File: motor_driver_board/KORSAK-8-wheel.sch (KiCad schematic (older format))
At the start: 26 parts, among them J1 Battery, J2 5V connector, J3 Logic Connector, J4 Charge Indicator, M1 Motor_DC, M2 Motor_DC, M3 Motor_DC, M4 Motor_DC, M5 Motor_DC, M6 Motor_DC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

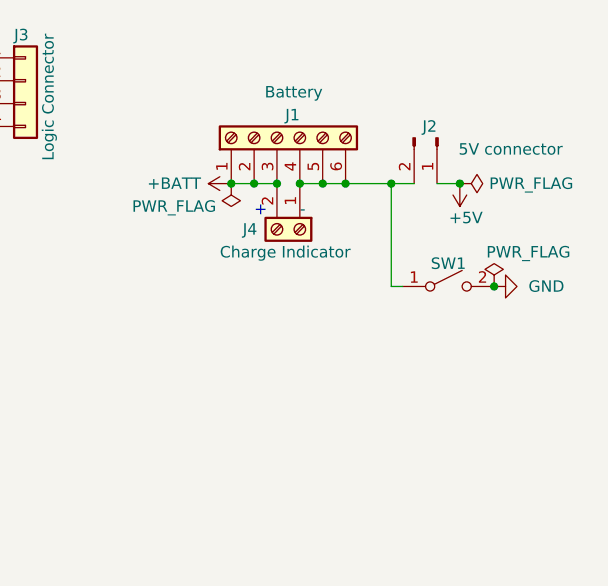
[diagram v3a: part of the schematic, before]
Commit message: Добавил вывод под зарядник
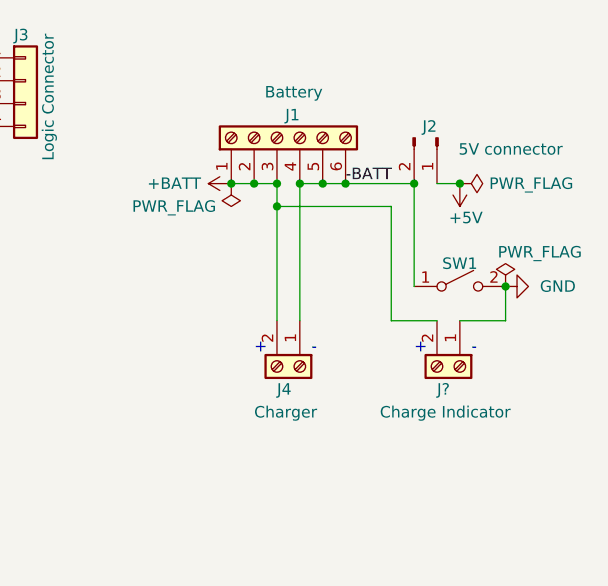
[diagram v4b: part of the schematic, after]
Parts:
- added J?: Charge Indicator, TerminalBlock_Phoenix:TerminalBlock_Phoenix_MKDS-1,5-2_1x02_P5.00mm_Horizontal, symbol Connector:Screw_Terminal_01x02
- J4: value Charge Indicator -> Charger
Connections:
- net +BATT: now also J?.2 (Pin_2)
- net GND: now also J?.1 (Pin_1)
- net -BATT: now reaches J1.4 (Pin_4), J1.5 (Pin_5), J1.6 (Pin_6), J2.2 (Pin_2), J4.1 (Pin_1), SW1.1 (A)
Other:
- moved on the sheet: J4, SW1
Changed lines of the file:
@@
 Title "KORSAK Motor Driver board"
 Date "2021-03-14"
-Rev "7"
+Rev "8"
 Comp ""
 Comment1 ""
@@
 L power:GND #PWR04
 U 1 1 5FFD08AA
-P 10200 4800
-F 0 "#PWR04" H 10200 4550 50  0001 C CNN
-F 1 "GND" V 10200 4650 50  0000 R CNN
-F 2 "" H 10200 4800 50  0001 C CNN
-F 3 "" H 10200 4800 50  0001 C CNN
-	1    10200 4800
+P 10250 4800
+F 0 "#PWR04" H 10250 4550 50  0001 C CNN
+F 1 "GND" V 10250 4650 50  0000 R CNN
+F 2 "" H 10250 4800 50  0001 C CNN
+F 3 "" H 10250 4800 50  0001 C CNN
+	1    10250 4800
 	0    -1   -1   0
 $EndComp
@@
 	4600 4900 4800 4900
 Connection ~ 9550 4350
-Connection ~ 9750 4350
-Wire Wire Line
-	9750 4350 9550 4350
+Connection ~ 9850 4350
+Wire Wire Line
+	9850 4350 9550 4350
 $Comp
 L power:PWR_FLAG #FLG0101
@@
 L power:PWR_FLAG #FLG0103
 U 1 1 60AE12BA
-P 10200 4800
-F 0 "#FLG0103" H 10200 4875 50  0001 C CNN
-F 1 "PWR_FLAG" H 10350 4950 50  0000 C CNN
-F 2 "" H 10200 4800 50  0001 C CNN
-F 3 "~" H 10200 4800 50  0001 C CNN
-	1    10200 4800
-	1    0    0    -1
-$EndComp
-Wire Wire Line
-	9750 4350 9850 4350
+P 10250 4800
+F 0 "#FLG0103" H 10250 4875 50  0001 C CNN
+F 1 "PWR_FLAG" H 10400 4950 50  0000 C CNN
+F 2 "" H 10250 4800 50  0001 C CNN
+F 3 "~" H 10250 4800 50  0001 C CNN
+	1    10250 4800
+	1    0    0    -1
+$EndComp
 $Comp
 L Switch:SW_SPST SW1
 U 1 1 604F19B3
-P 10000 4800
-F 0 "SW1" H 10000 4900 50  0000 C CNN
-F 1 "SW_SPST" H 10000 4700 50  0001 C CNN
-F 2 "TerminalBlock_Phoenix:TerminalBlock_Phoenix_MKDS-1,5-2_1x02_P5.00mm_Horizontal" H 10000 4800 50  0001 C CNN
-F 3 "~" H 10000 4800 50  0001 C CNN
-	1    10000 4800
-	1    0    0    -1
-$EndComp
-Connection ~ 9250 4350
-Connection ~ 10200 4800
-Wire Wire Line
-	9750 4350 9750 4800
-Wire Wire Line
-	9750 4800 9800 4800
+P 10050 4800
+F 0 "SW1" H 10050 4900 50  0000 C CNN
+F 1 "SW_SPST" H 10050 4700 50  0001 C CNN
+F 2 "TerminalBlock_Phoenix:TerminalBlock_Phoenix_MKDS-1,5-2_1x02_P5.00mm_Horizontal" H 10050 4800 50  0001 C CNN
+F 3 "~" H 10050 4800 50  0001 C CNN
+	1    10050 4800
+	1    0    0    -1
+$EndComp
+Connection ~ 10250 4800
+Wire Wire Line
+	9850 4350 9850 4800
 $Comp
 L Connector:Screw_Terminal_01x02 J4
 U 1 1 6053A604
-P 9350 4550
-F 0 "J4" V 9350 4300 50  0000 L CNN
-F 1 "Charge Indicator" V 9450 4200 50  0000 L CNN
-F 2 "TerminalBlock_Phoenix:TerminalBlock_Phoenix_MKDS-1,5-2_1x02_P5.00mm_Horizontal" H 9350 4550 50  0001 C CNN
-F 3 "~" H 9350 4550 50  0001 C CNN
-	1    9350 4550
+P 9350 5150
+F 0 "J4" V 9450 5050 50  0000 L CNN
+F 1 "Charger" V 9550 4950 50  0000 L CNN
+F 2 "TerminalBlock_Phoenix:TerminalBlock_Phoenix_MKDS-1,5-2_1x02_P5.00mm_Horizontal" H 9350 5150 50  0001 C CNN
+F 3 "~" H 9350 5150 50  0001 C CNN
+	1    9350 5150
 	0    1    1    0
 $EndComp
-Connection ~ 9350 4350
-Text Notes 9350 4500 0    50   ~ 0
+Text Notes 10100 5100 0    50   ~ 0
 -
-Text Notes 9150 4500 0    50   ~ 0
+Text Notes 9850 5100 0    50   ~ 0
 +
 Wire Wire Line
@@
 Text Label 7950 4100 2    50   ~ 0
 R_IN_1
+Text Label 9550 4350 0    50   ~ 0
+-BATT
+$Comp
+L Connector:Screw_Terminal_01x02 J?
+U 1 1 609ED073
+P 10050 5150
+F 0 "J?" V 10150 5050 50  0000 L CNN
+F 1 "Charge Indicator" V 10250 4800 50  0000 L CNN
+F 2 "TerminalBlock_Phoenix:TerminalBlock_Phoenix_MKDS-1,5-2_1x02_P5.00mm_Horizontal" H 10050 5150 50  0001 C CNN
+F 3 "~" H 10050 5150 50  0001 C CNN
+	1    10050 5150
+	0    1    1    0
+$EndComp
+Wire Wire Line
+	10250 4800 10250 4950
+Wire Wire Line
+	10250 4950 10050 4950
+Wire Wire Line
+	9950 4950 9750 4950
+Wire Wire Line
+	9750 4950 9750 4450
+Wire Wire Line
+	9750 4450 9250 4450
+Wire Wire Line
+	9250 4450 9250 4350
+Connection ~ 9250 4350
+Wire Wire Line
+	9250 4950 9250 4450
+Connection ~ 9250 4450
+Wire Wire Line
+	9350 4950 9350 4350
+Connection ~ 9350 4350
+Text Notes 9150 5100 0    50   ~ 0
++
+Text Notes 9400 5100 0    50   ~ 0
+-
 $EndSCHEMATC

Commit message: Закончил моделировать плату
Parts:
- removed J2: 5V connector, Connector_PinHeader_2.54mm:PinHeader_1x02_P2.54mm_Horizontal, symbol Connector:Conn_01x02_Male
- added J2: 5V Power, TerminalBlock_Phoenix:TerminalBlock_Phoenix_MKDS-1,5-2_1x02_P5.00mm_Horizontal, symbol Connector:Screw_Terminal_01x02
- added unit 7 of U5
- gave numbers to parts that had none: 1
- renumbered C5 to C3, C6 to C4, C3 to C5, C4 to C6, U4 to U2, U2 to U4
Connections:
- net +5V: now also J2.2 (Pin_2), U5.14 (VCC)
- net -BATT: now also J2.1 (Pin_1)
- net GND: now also U5.7 (GND)
- net L_IN_1: now also U3.15 (4A), U4.15 (4A); no longer U3.10 (3A), U4.10 (3A)
- net L_IN_2: now also U3.10 (3A), U4.10 (3A); no longer U3.15 (4A), U4.15 (4A)
- net M5_OUT_1: now also C6.2, M6.1 (+); no longer C5.2, M5.1 (+)
- net M5_OUT_2: now also C6.1, M6.2 (-); no longer C5.1, M5.2 (-)
- net M6_OUT_1: now also C5.2, M5.1 (+); no longer C6.2, M6.1 (+)
- net M6_OUT_2: now also C5.1, M5.2 (-); no longer C6.1, M6.2 (-)
- net M7_OUT_1: now also C8.2, M8.1 (+); no longer C7.2, M7.1 (+)
- net M7_OUT_2: now also C8.1, M8.2 (-); no longer C7.1, M7.2 (-)
- net M8_OUT_1: now also C7.2, M7.1 (+); no longer C8.2, M8.1 (+)
- net M8_OUT_2: now also C7.1, M7.2 (-); no longer C8.1, M8.2 (-)
- net R_IN_1: now also U1.15 (4A), U2.15 (4A); no longer U1.10 (3A), U2.10 (3A)
- net R_IN_2: now also U1.10 (3A), U2.10 (3A); no longer U1.15 (4A), U2.15 (4A)
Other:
- moved on the sheet: C5, C6, C7, C8, M5, M6, M7, M8
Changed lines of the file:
@@
 L Motor:Motor_DC M8
 U 1 1 601FA19C
+P 5550 5500
+F 0 "M8" V 5350 5400 50  0000 L CNN
+F 1 "Motor_DC" V 5750 5300 50  0000 L CNN
+F 2 "TerminalBlock_Phoenix:TerminalBlock_Phoenix_MKDS-1,5-2_1x02_P5.00mm_Horizontal" H 5550 5410 50  0001 C CNN
+F 3 "~" H 5550 5410 50  0001 C CNN
+	1    5550 5500
+	1    0    0    -1
+$EndComp
+$Comp
+L Motor:Motor_DC M7
+U 1 1 601FA1A6
 P 5550 4900
-F 0 "M8" V 5350 4800 50  0000 L CNN
+F 0 "M7" V 5350 4800 50  0000 L CNN
 F 1 "Motor_DC" V 5750 4700 50  0000 L CNN
 F 2 "TerminalBlock_Phoenix:TerminalBlock_Phoenix_MKDS-1,5-2_1x02_P5.00mm_Horizontal" H 5550 4810 50  0001 C CNN
 F 3 "~" H 5550 4810 50  0001 C CNN
 	1    5550 4900
-	1    0    0    -1
-$EndComp
-$Comp
-L Motor:Motor_DC M7
-U 1 1 601FA1A6
-P 5550 5500
-F 0 "M7" V 5350 5400 50  0000 L CNN
-F 1 "Motor_DC" V 5750 5300 50  0000 L CNN
-F 2 "TerminalBlock_Phoenix:TerminalBlock_Phoenix_MKDS-1,5-2_1x02_P5.00mm_Horizontal" H 5550 5410 50  0001 C CNN
-F 3 "~" H 5550 5410 50  0001 C CNN
-	1    5550 5500
 	1    0    0    -1
 $EndComp
@@
 $EndComp
 $Comp
-L Driver_Motor:L293D U2
+L Driver_Motor:L293D U4
 U 1 1 601FA21D
 P 4100 5300
-F 0 "U2" H 4250 5600 50  0000 C CNN
+F 0 "U4" H 4250 5600 50  0000 C CNN
 F 1 "L293D" H 4250 5450 50  0000 C CNN
 F 2 "Package_DIP:DIP-16_W7.62mm_Socket_LongPads" H 4350 4550 50  0001 L CNN
@@
 	1    4100 5300
 	1    0    0    -1
-$EndComp
-$Comp
-L Connector:Conn_01x02_Male J2
-U 1 1 60435B47
-P 9950 4150
-F 0 "J2" V 9900 4150 50  0000 R CNN
-F 1 "5V connector" V 10000 4700 50  0000 R CNN
-F 2 "Connector_PinHeader_2.54mm:PinHeader_1x02_P2.54mm_Horizontal" H 9950 4150 50  0001 C CNN
-F 3 "~" H 9950 4150 50  0001 C CNN
-	1    9950 4150
-	0    1    1    0
 $EndComp
 Wire Wire Line
@@
 L Device:C C7
 U 1 1 60A139F7
+P 5000 4950
+F 0 "C7" H 5115 4996 50  0000 L CNN
+F 1 "10pF" H 5115 4905 50  0000 L CNN
+F 2 "Capacitor_THT:C_Disc_D5.0mm_W2.5mm_P5.00mm" H 5038 4800 50  0001 C CNN
+F 3 "~" H 5000 4950 50  0001 C CNN
+	1    5000 4950
+	1    0    0    1
+$EndComp
+$Comp
+L Device:C C8
+U 1 1 60A183A3
 P 5000 5550
-F 0 "C7" H 5115 5596 50  0000 L CNN
+F 0 "C8" H 5115 5596 50  0000 L CNN
 F 1 "10pF" H 5115 5505 50  0000 L CNN
 F 2 "Capacitor_THT:C_Disc_D5.0mm_W2.5mm_P5.00mm" H 5038 5400 50  0001 C CNN
@@
 	1    0    0    1
 $EndComp
-$Comp
-L Device:C C8
-U 1 1 60A183A3
-P 5000 4950
-F 0 "C8" H 5115 4996 50  0000 L CNN
-F 1 "10pF" H 5115 4905 50  0000 L CNN
-F 2 "Capacitor_THT:C_Disc_D5.0mm_W2.5mm_P5.00mm" H 5038 4800 50  0001 C CNN
-F 3 "~" H 5000 4950 50  0001 C CNN
-	1    5000 4950
-	1    0    0    1
-$EndComp
 Wire Wire Line
 	5000 5700 5000 5800
@@
 	4600 4900 4800 4900
 Connection ~ 9550 4350
-Connection ~ 9850 4350
 Wire Wire Line
 	9850 4350 9550 4350
@@
 	1550 5300 1000 5300
 Connection ~ 1550 5300
-Wire Wire Line
-	1550 5400 1550 5300
 $Comp
 L Device:C C1
@@
 $EndComp
 $Comp
-L Device:C C3
+L Device:C C5
 U 1 1 60A267CC
+P 1550 4950
+F 0 "C5" H 1665 4996 50  0000 L CNN
+F 1 "10pF" H 1665 4905 50  0000 L CNN
+F 2 "Capacitor_THT:C_Disc_D5.0mm_W2.5mm_P5.00mm" H 1588 4800 50  0001 C CNN
+F 3 "~" H 1550 4950 50  0001 C CNN
+	1    1550 4950
+	-1   0    0    1
+$EndComp
+$Comp
+L Device:C C6
+U 1 1 60A1E5A3
 P 1550 5550
-F 0 "C3" H 1665 5596 50  0000 L CNN
+F 0 "C6" H 1665 5596 50  0000 L CNN
 F 1 "10pF" H 1665 5505 50  0000 L CNN
 F 2 "Capacitor_THT:C_Disc_D5.0mm_W2.5mm_P5.00mm" H 1588 5400 50  0001 C CNN
 F 3 "~" H 1550 5550 50  0001 C CNN
 	1    1550 5550
-	-1   0    0    1
-$EndComp
-$Comp
-L Device:C C4
-U 1 1 60A1E5A3
-P 1550 4950
-F 0 "C4" H 1665 4996 50  0000 L CNN
-F 1 "10pF" H 1665 4905 50  0000 L CNN
-F 2 "Capacitor_THT:C_Disc_D5.0mm_W2.5mm_P5.00mm" H 1588 4800 50  0001 C CNN
-F 3 "~" H 1550 4950 50  0001 C CNN
-	1    1550 4950
 	-1   0    0    1
 $EndComp
@@
 L Motor:Motor_DC M6
 U 1 1 601FA1F2
-P 1000 4900
-F 0 "M6" V 1200 4800 50  0000 L CNN
-F 1 "Motor_DC" V 800 4700 50  0000 L CNN
-F 2 "TerminalBlock_Phoenix:TerminalBlock_Phoenix_MKDS-1,5-2_1x02_P5.00mm_Horizontal" H 1000 4810 50  0001 C CNN
-F 3 "~" H 1000 4810 50  0001 C CNN
-	1    1000 4900
+P 1000 5500
+F 0 "M6" V 1200 5400 50  0000 L CNN
+F 1 "Motor_DC" V 800 5300 50  0000 L CNN
+F 2 "TerminalBlock_Phoenix:TerminalBlock_Phoenix_MKDS-1,5-2_1x02_P5.00mm_Horizontal" H 1000 5410 50  0001 C CNN
+F 3 "~" H 1000 5410 50  0001 C CNN
+	1    1000 5500
 	1    0    0    -1
 $EndComp
@@
 L Motor:Motor_DC M5
 U 1 1 601FA1E8
-P 1000 5500
-F 0 "M5" V 800 5400 50  0000 L CNN
-F 1 "Motor_DC" V 1200 5300 50  0000 L CNN
-F 2 "TerminalBlock_Phoenix:TerminalBlock_Phoenix_MKDS-1,5-2_1x02_P5.00mm_Horizontal" H 1000 5410 50  0001 C CNN
-F 3 "~" H 1000 5410 50  0001 C CNN
-	1    1000 5500
+P 1000 4900
+F 0 "M5" V 800 4800 50  0000 L CNN
+F 1 "Motor_DC" V 1200 4700 50  0000 L CNN
+F 2 "TerminalBlock_Phoenix:TerminalBlock_Phoenix_MKDS-1,5-2_1x02_P5.00mm_Horizontal" H 1000 4810 50  0001 C CNN
+F 3 "~" H 1000 4810 50  0001 C CNN
+	1    1000 4900
 	-1   0    0    -1
 $EndComp
@@
 Wire Wire Line
 	2950 5700 3600 5700
-Text Label 3150 5300 0    50   ~ 0
+Text Label 3150 5500 0    50   ~ 0
 L_IN_1
 Text Label 3150 4700 0    50   ~ 0
@@
 Text Label 3150 4900 0    50   ~ 0
 L_IN_2
-Text Label 3150 5500 0    50   ~ 0
+Text Label 3150 5300 0    50   ~ 0
 L_IN_2
 Text Label 3150 5700 0    50   ~ 0
@@
 Text Label 3150 2350 0    50   ~ 0
 R_IN_1
-Text Label 3150 2950 0    50   ~ 0
+Text Label 3150 3150 0    50   ~ 0
 R_IN_1
 Text Label 3150 2550 0    50   ~ 0
 R_IN_2
-Text Label 3150 3150 0    50   ~ 0
+Text Label 3150 2950 0    50   ~ 0
 R_IN_2
 $Comp
@@
 	5000 2950 5000 3050
 $Comp
-L Device:C C6
+L Device:C C4
 U 1 1 60A02B64
 P 5000 3200
-F 0 "C6" H 5115 3246 50  0000 L CNN
+F 0 "C4" H 5115 3246 50  0000 L CNN
 F 1 "10pF" H 5115 3155 50  0000 L CNN
 F 2 "Capacitor_THT:C_Disc_D5.0mm_W2.5mm_P5.00mm" H 5038 3050 50  0001 C CNN
@@
 	5000 2750 5000 2850
 $Comp
-L Device:C C5
+L Device:C C3
 U 1 1 609F73D7
 P 5000 2600
-F 0 "C5" H 5115 2646 50  0000 L CNN
+F 0 "C3" H 5115 2646 50  0000 L CNN
 F 1 "10pF" H 5115 2555 50  0000 L CNN
 F 2 "Capacitor_THT:C_Disc_D5.0mm_W2.5mm_P5.00mm" H 5038 2450 50  0001 C CNN
@@
 	4800 2550 4800 2850
 $Comp
-L Driver_Motor:L293D U4
+L Driver_Motor:L293D U2
 U 1 1 5F9AC5A8
 P 4050 2950
-F 0 "U4" H 4200 3250 50  0000 C CNN
+F 0 "U2" H 4200 3250 50  0000 C CNN
 F 1 "L293D" H 4200 3100 50  0000 C CNN
 F 2 "Package_DIP:DIP-16_W7.62mm_Socket_LongPads" H 4300 2200 50  0001 L CNN
@@
 -BATT
 $Comp
-L Connector:Screw_Terminal_01x02 J?
+L Connector:Screw_Terminal_01x02 J5
 U 1 1 609ED073
 P 10050 5150
-F 0 "J?" V 10150 5050 50  0000 L CNN
+F 0 "J5" V 10150 5050 50  0000 L CNN
 F 1 "Charge Indicator" V 10250 4800 50  0000 L CNN
 F 2 "TerminalBlock_Phoenix:TerminalBlock_Phoenix_MKDS-1,5-2_1x02_P5.00mm_Horizontal" H 10050 5150 50  0001 C CNN
@@
 Text Notes 9400 5100 0    50   ~ 0
 -
+Wire Wire Line
+	1550 5300 1550 5400
+$Comp
+L Connector:Screw_Terminal_01x02 J2
+U 1 1 60B0E0CC
+P 9850 4150
+F 0 "J2" V 9814 3962 50  0000 R CNN
+F 1 "5V Power" V 9950 4250 50  0000 R CNN
+F 2 "TerminalBlock_Phoenix:TerminalBlock_Phoenix_MKDS-1,5-2_1x02_P5.00mm_Horizontal" H 9850 4150 50  0001 C CNN
+F 3 "~" H 9850 4150 50  0001 C CNN
+	1    9850 4150
+	0    -1   -1   0
+$EndComp
+Connection ~ 9850 4350
+$Comp
+L 74xx:74LS04 U5
+U 7 1 60B55850
+P 7400 4700
+F 0 "U5" V 7033 4700 50  0000 C CNN
+F 1 "74LS04" V 7124 4700 50  0000 C CNN
+F 2 "" H 7400 4700 50  0001 C CNN
+F 3 "http://www.ti.com/lit/gpn/sn74LS04" H 7400 4700 50  0001 C CNN
+	7    7400 4700
+	0    1    1    0
+$EndComp
+$Comp
+L power:+5V #PWR?
+U 1 1 60B5896B
+P 7900 4700
+F 0 "#PWR?" H 7900 4550 50  0001 C CNN
+F 1 "+5V" V 7915 4828 50  0000 L CNN
+F 2 "" H 7900 4700 50  0001 C CNN
+F 3 "" H 7900 4700 50  0001 C CNN
+	1    7900 4700
+	0    1    1    0
+$EndComp
+$Comp
+L power:GND #PWR?
+U 1 1 60B59733
+P 6900 4700
+F 0 "#PWR?" H 6900 4450 50  0001 C CNN
+F 1 "GND" V 6905 4572 50  0000 R CNN
+F 2 "" H 6900 4700 50  0001 C CNN
+F 3 "" H 6900 4700 50  0001 C CNN
+	1    6900 4700
+	0    1    1    0
+$EndComp
 $EndSCHEMATC
